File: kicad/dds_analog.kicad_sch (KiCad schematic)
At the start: 61 parts, among them J1 Conn_Coaxial, U1 AD9954, U2 OPA859xDSG, U8 OPA859xDSG, X1 ASE-xxxMHz

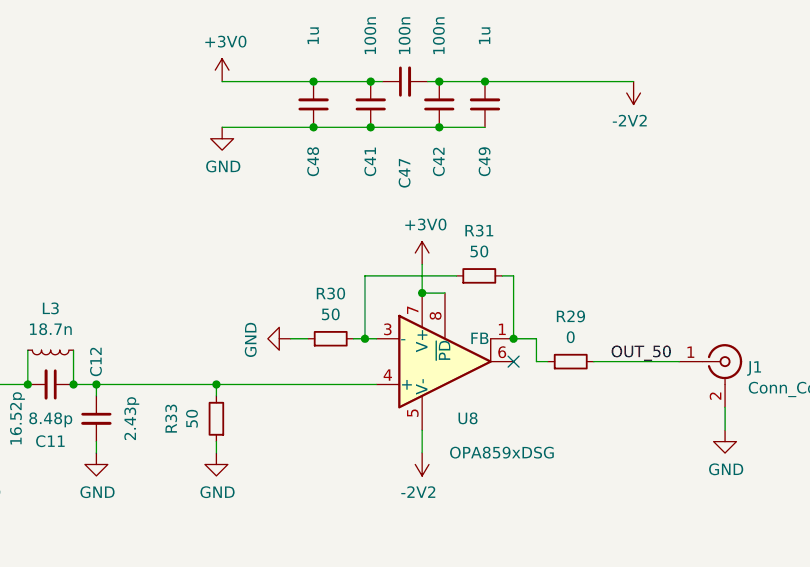
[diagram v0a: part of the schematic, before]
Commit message: prepare for jlcpcb order (v2)
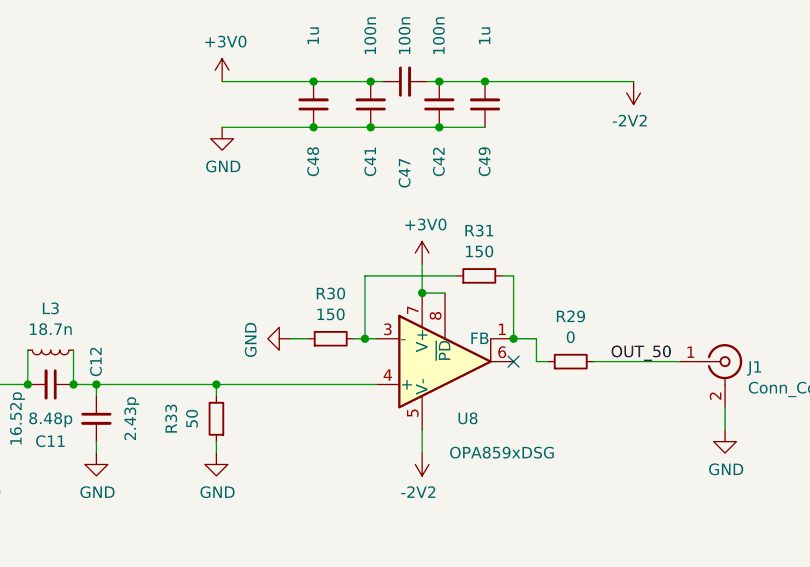
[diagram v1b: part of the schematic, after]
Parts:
- R30, R31: value 50 -> 150
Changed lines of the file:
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@@
     (effects (font (size 1.27 1.27)) (justify left bottom))
   )
-  (label "OUT_50" (at 260.35 109.855 0)
+  (label "OUT_50" (at 260.35 109.855 0) (fields_autoplaced)
     (effects (font (size 1.27 1.27)) (justify left bottom))
   )
@@
   (symbol (lib_id "power:GND") (at 273.05 117.475 0) (unit 1)
     (in_bom yes) (on_board yes) (dnp no)
-    (property "Reference" "#PWR?" (at 273.05 123.825 0)
+    (property "Reference" "#PWR033" (at 273.05 123.825 0)
       (effects (font (size 1.27 1.27)) hide)
     )
@@
       (effects (font (size 1.27 1.27)))
     )
-    (property "Value" "50" (at 245.745 97.663 90)
+    (property "Value" "150" (at 245.745 97.663 90)
       (effects (font (size 1.27 1.27)))
     )
@@
       (effects (font (size 1.27 1.27)))
     )
-    (property "Value" "50" (at 229.235 104.648 90)
-      (effects (font (size 1.27 1.27)))
-    )
+    (property "Value" "150" (at 229.235 104.648 90)
+      (effects (font (size 1.27 1.27)))
+    )

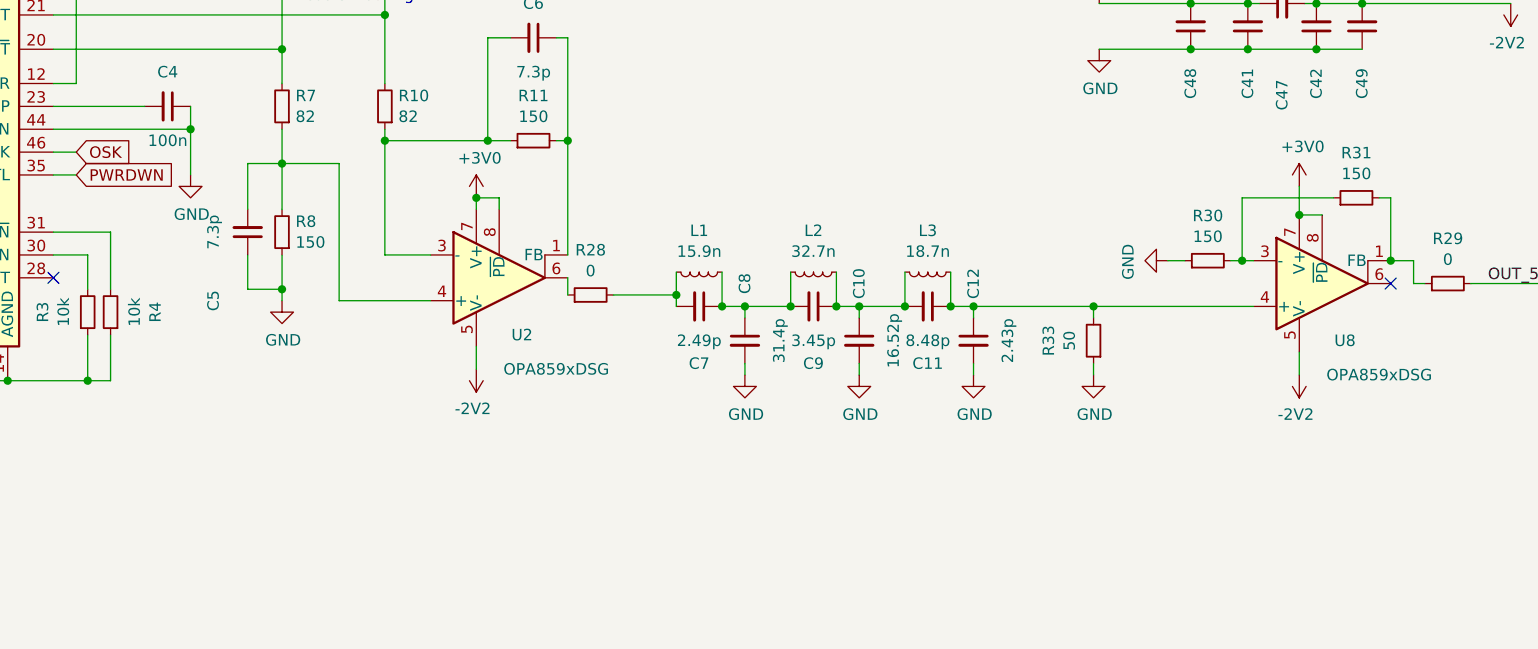
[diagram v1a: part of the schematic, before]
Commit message: modified a few values (as loaded on v2 prototype board)
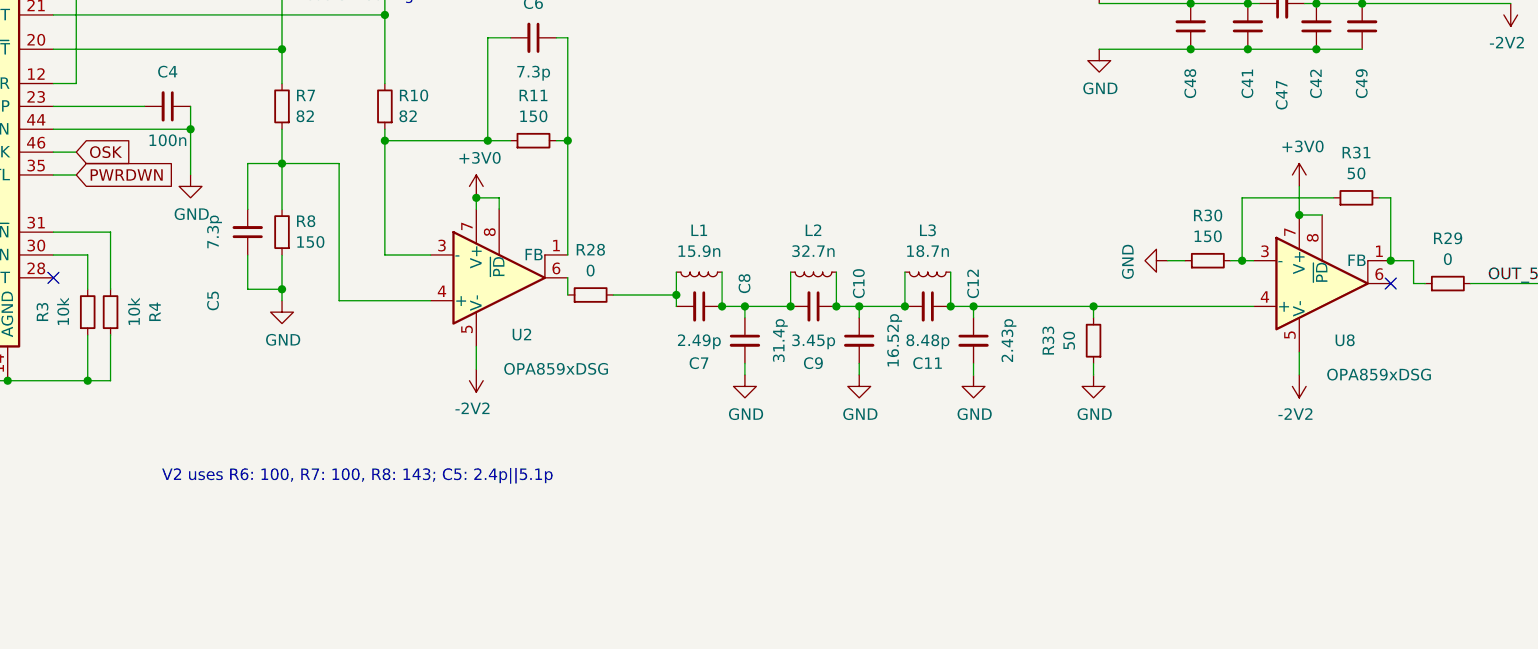
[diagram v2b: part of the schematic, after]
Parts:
- R31: value 150 -> 50
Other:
- note added: "V2 uses R6: 100, R7: 100, R8: 143; C5: 2.4p||5.1p"
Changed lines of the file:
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@@
     (stroke (width 0) (type default))
+  )
+  (text "V2 uses R6: 100, R7: 100, R8: 143; C5: 2.4p||5.1p" (at 113.03 132.08 0)
+    (effects (font (size 1.27 1.27)) (justify left bottom))
   )
   (text "Output phase\ninverted for \neasier routing" (at 128.905 78.74 0)
@@
       (effects (font (size 1.27 1.27)))
     )
-    (property "Value" "150" (at 245.745 97.663 90)
-      (effects (font (size 1.27 1.27)))
-    )
+    (property "Value" "50" (at 245.745 97.663 90)
+      (effects (font (size 1.27 1.27)))
+    )

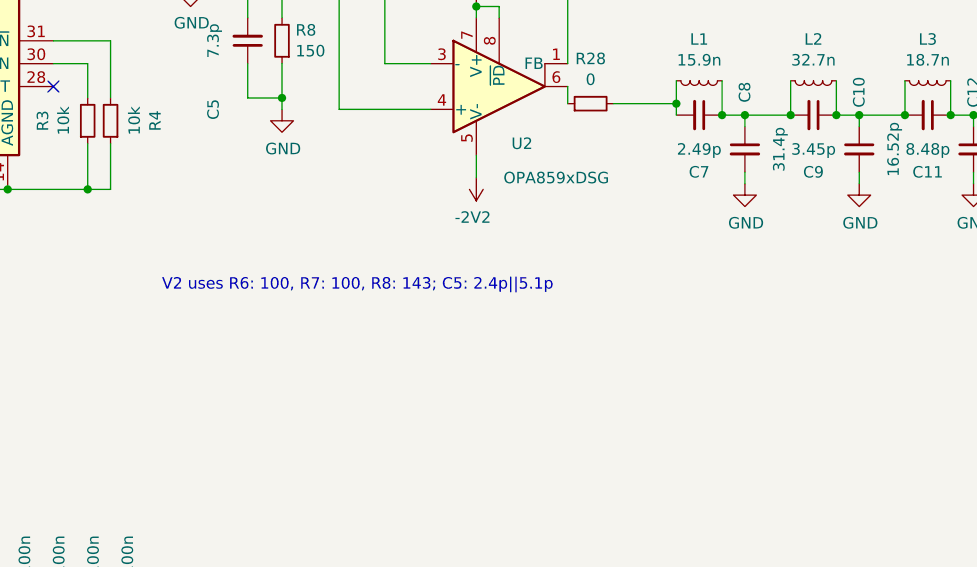
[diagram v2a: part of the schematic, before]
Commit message: emphasize that the values are for the V2 *prototype*
The final version uses different voltages: 2.8/-2.4 (vs 3.0/-2.2).
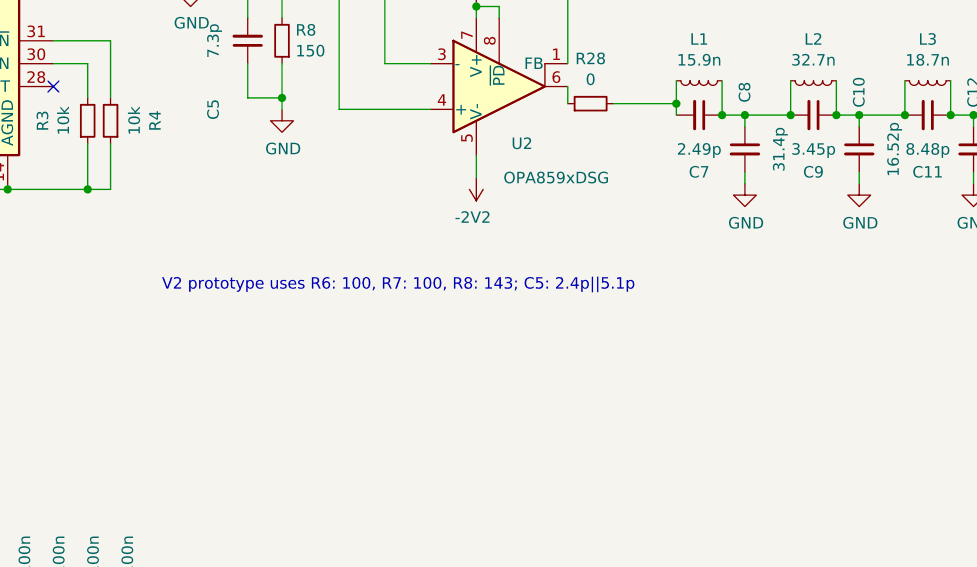
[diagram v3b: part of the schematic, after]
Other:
- note added: "V2 prototype uses R6: 100, R7: 100, R8: 143; C5: 2.4p||5.1p"
- note removed: "V2 uses R6: 100, R7: 100, R8: 143; C5: 2.4p||5.1p"
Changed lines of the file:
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@@
     (stroke (width 0) (type default))
   )
-  (text "V2 uses R6: 100, R7: 100, R8: 143; C5: 2.4p||5.1p" (at 113.03 132.08 0)
+  (text "V2 prototype uses R6: 100, R7: 100, R8: 143; C5: 2.4p||5.1p"
+    (at 113.03 132.08 0)
     (effects (font (size 1.27 1.27)) (justify left bottom))
   )

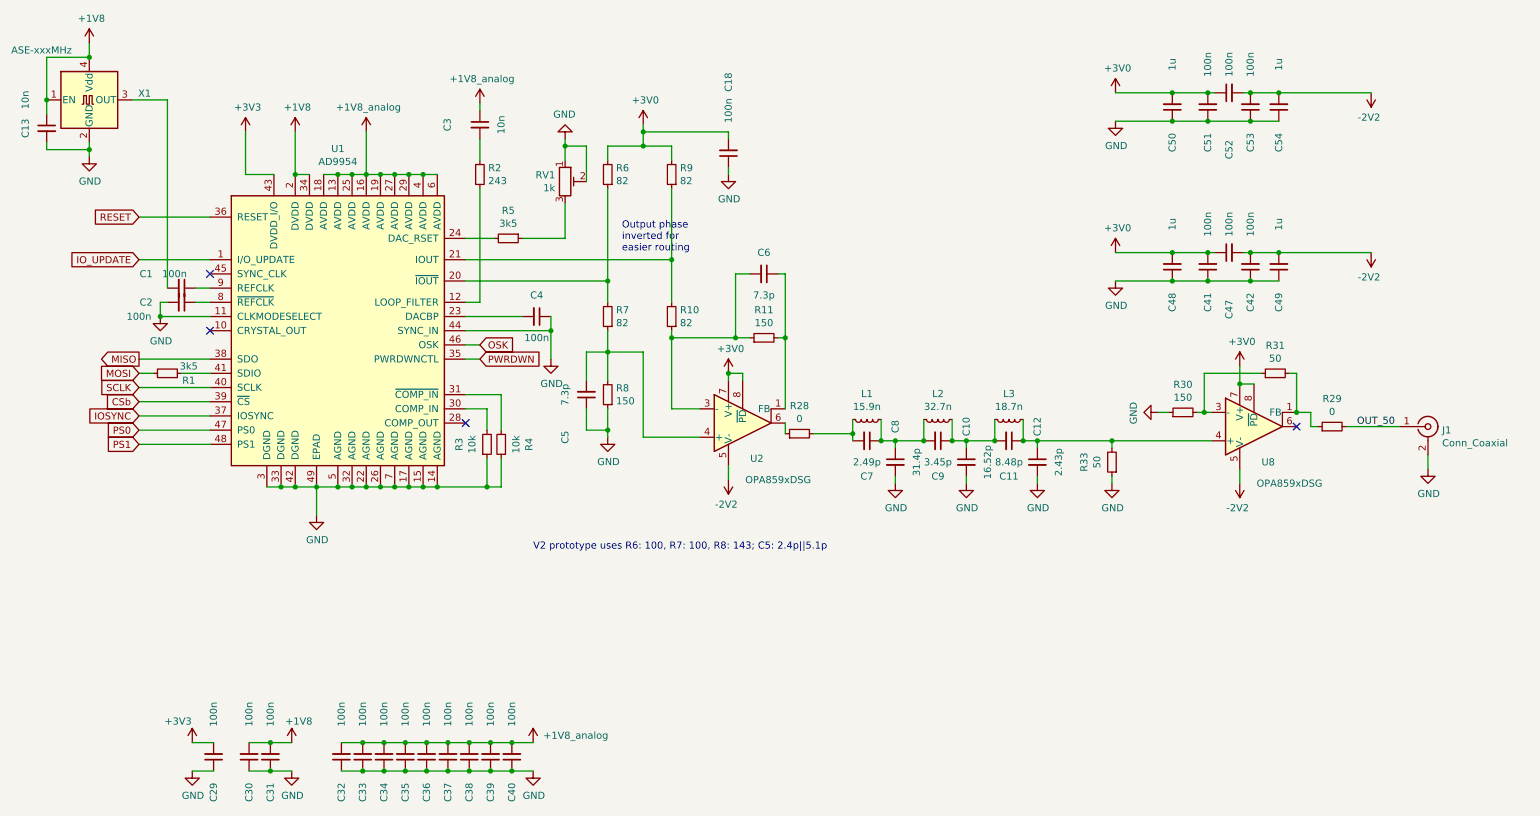
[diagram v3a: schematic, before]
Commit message: changed values in schematic for v2 board
Most notably: moved from +3.0/-2.2V to +2.8/-2.4V analog supply.
This required changing the diff-amp resistors to stay within
the common-mode range of the AD9954 and the OPA859.
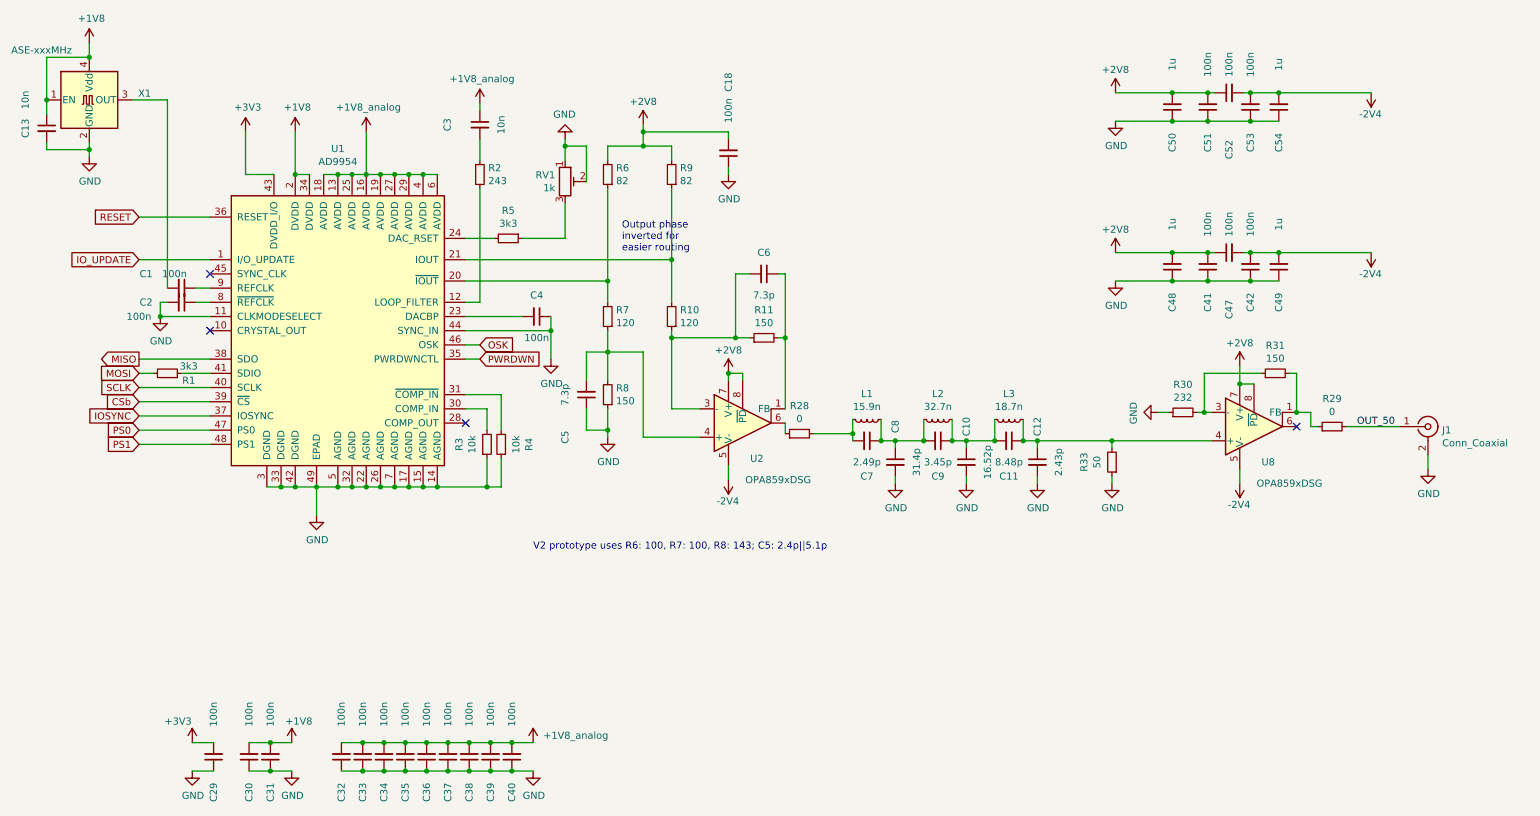
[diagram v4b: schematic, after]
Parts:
- R1, R5: value 3k5 -> 3k3
- R10, R7: value 82 -> 120
- R30: value 150 -> 232
- R31: value 50 -> 150
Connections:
- net +3V0 renamed +2V8
- net -2V2 renamed -2V4
